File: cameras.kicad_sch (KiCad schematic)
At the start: 30 parts

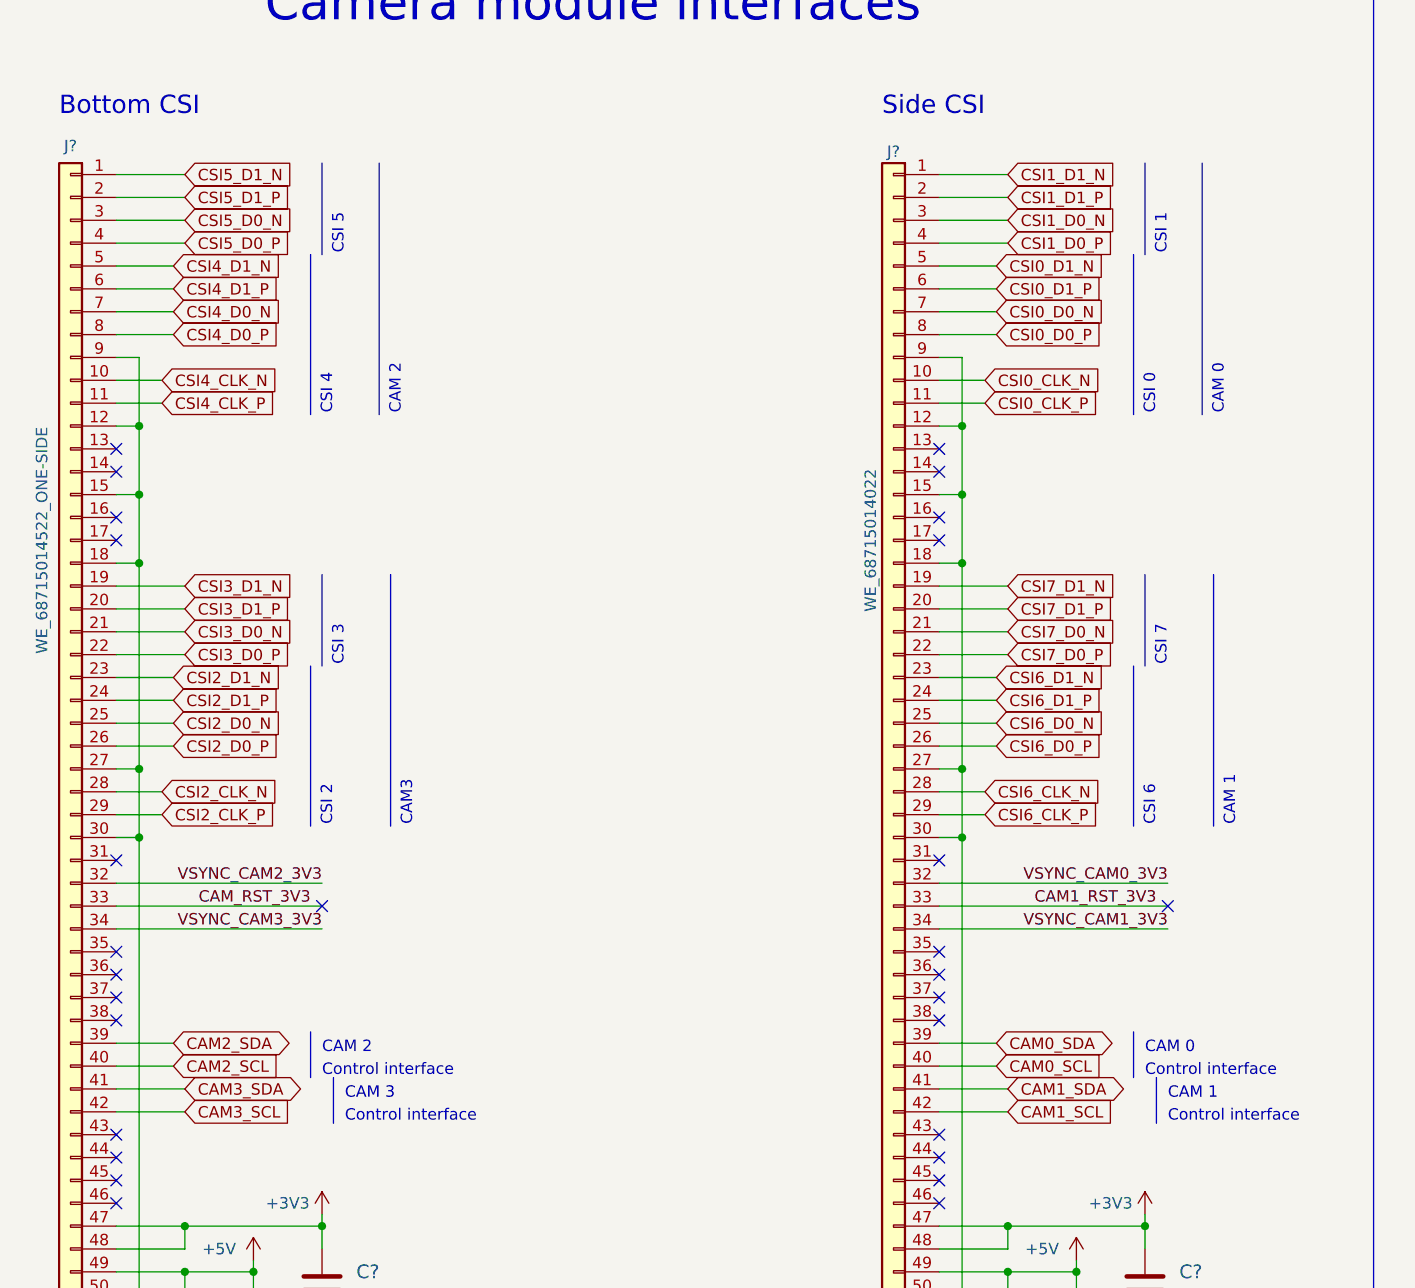
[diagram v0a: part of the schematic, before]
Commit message: Changed pinout to match Jetson Nano Baseboard
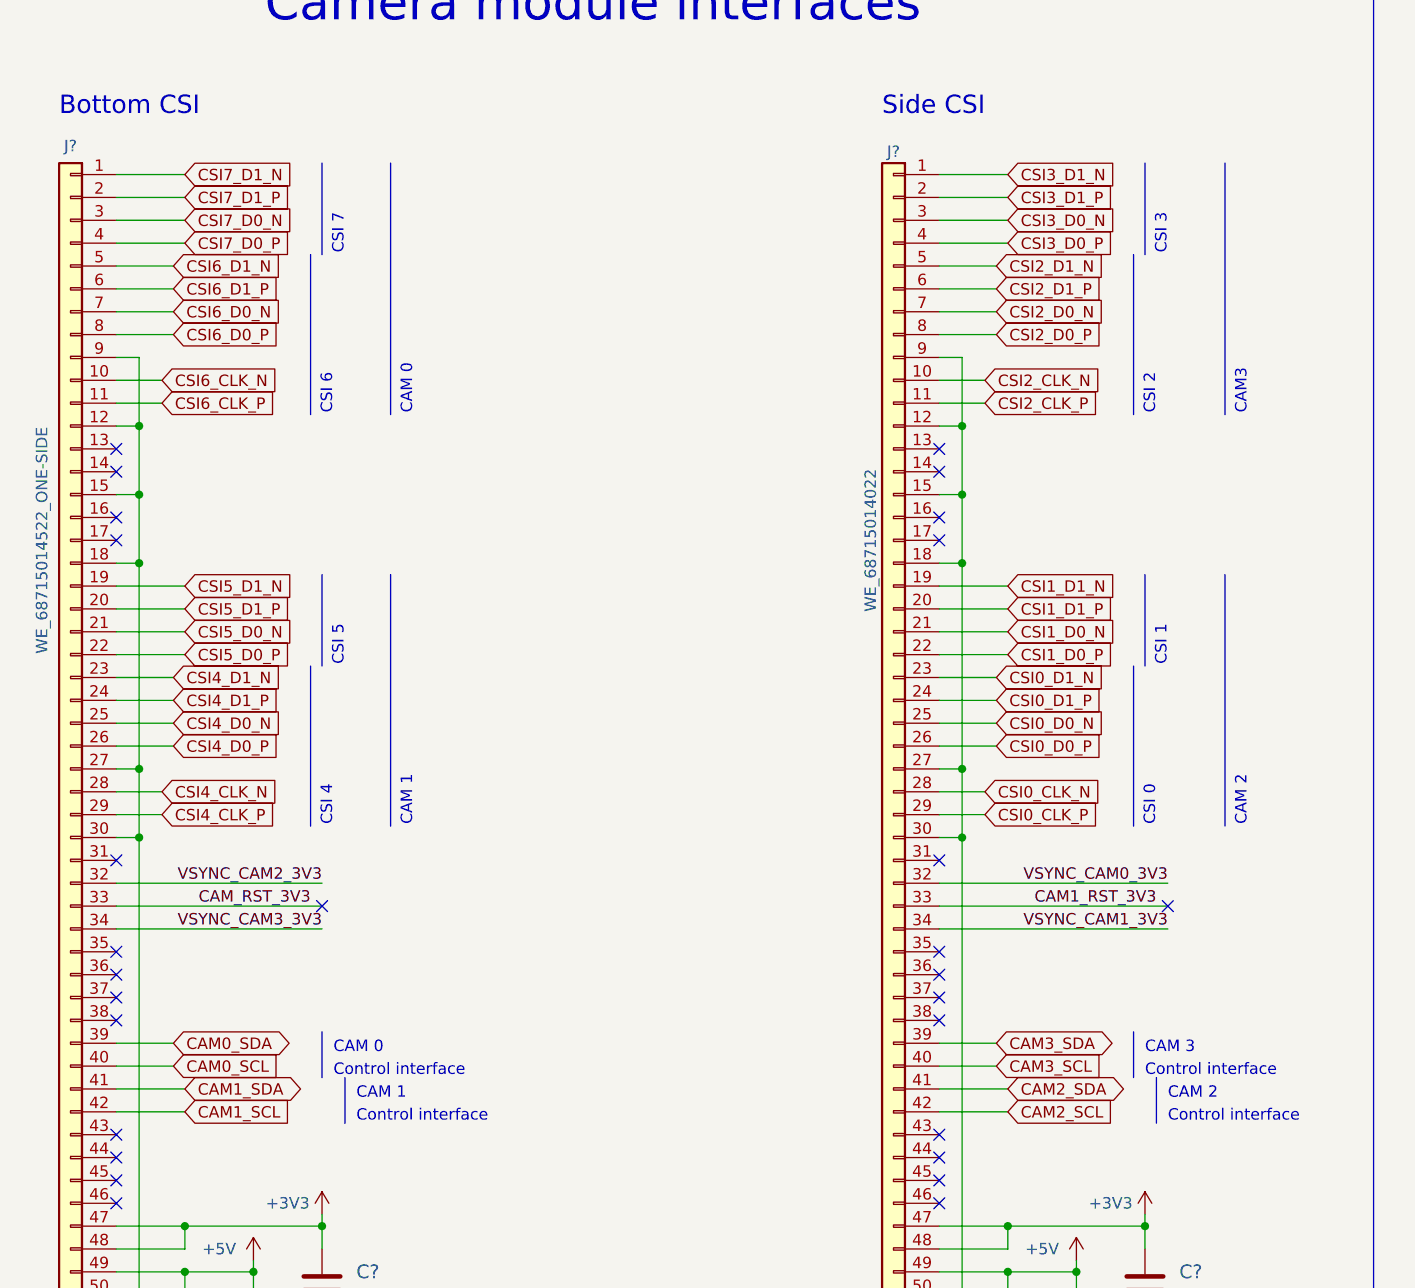
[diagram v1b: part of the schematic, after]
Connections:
- net CAM0_SCL: now also J?.40 (Pin_40); no longer J?.40 (Pin_40)
- net CAM0_SDA: now also J?.39 (Pin_39); no longer J?.39 (Pin_39)
- net CAM1_SCL: now also J?.42 (Pin_42); no longer J?.42 (Pin_42)
- net CAM1_SDA: now also J?.41 (Pin_41); no longer J?.41 (Pin_41)
- net CAM2_SCL: now also J?.42 (Pin_42); no longer J?.40 (Pin_40)
- net CAM2_SDA: now also J?.41 (Pin_41); no longer J?.39 (Pin_39)
- net CAM3_SCL: now also J?.40 (Pin_40); no longer J?.42 (Pin_42)
- net CAM3_SDA: now also J?.39 (Pin_39); no longer J?.41 (Pin_41)
- net CSI0_CLK_N: now also J?.28 (Pin_28); no longer J?.10 (Pin_10)
- net CSI0_CLK_P: now also J?.29 (Pin_29); no longer J?.11 (Pin_11)
- net CSI0_D0_N: now also J?.25 (Pin_25); no longer J?.7 (Pin_7)
- net CSI0_D0_P: now also J?.26 (Pin_26); no longer J?.8 (Pin_8)
- net CSI0_D1_N: now also J?.23 (Pin_23); no longer J?.5 (Pin_5)
- net CSI0_D1_P: now also J?.24 (Pin_24); no longer J?.6 (Pin_6)
- net CSI1_D0_N: now also J?.21 (Pin_21); no longer J?.3 (Pin_3)
- net CSI1_D0_P: now also J?.22 (Pin_22); no longer J?.4 (Pin_4)
- net CSI1_D1_N: now also J?.19 (Pin_19); no longer J?.1 (Pin_1)
- net CSI1_D1_P: now also J?.20 (Pin_20); no longer J?.2 (Pin_2)
- net CSI2_CLK_N: now also J?.10 (Pin_10); no longer J?.28 (Pin_28)
- net CSI2_CLK_P: now also J?.11 (Pin_11); no longer J?.29 (Pin_29)
- net CSI2_D0_N: now also J?.7 (Pin_7); no longer J?.25 (Pin_25)
- net CSI2_D0_P: now also J?.8 (Pin_8); no longer J?.26 (Pin_26)
- net CSI2_D1_N: now also J?.5 (Pin_5); no longer J?.23 (Pin_23)
- net CSI2_D1_P: now also J?.6 (Pin_6); no longer J?.24 (Pin_24)
- net CSI3_D0_N: now also J?.3 (Pin_3); no longer J?.21 (Pin_21)
- net CSI3_D0_P: now also J?.4 (Pin_4); no longer J?.22 (Pin_22)
- net CSI3_D1_N: now also J?.1 (Pin_1); no longer J?.19 (Pin_19)
- net CSI3_D1_P: now also J?.2 (Pin_2); no longer J?.20 (Pin_20)
- net CSI4_CLK_N: now also J?.28 (Pin_28); no longer J?.10 (Pin_10)
- net CSI4_CLK_P: now also J?.29 (Pin_29); no longer J?.11 (Pin_11)
- net CSI4_D0_N: now also J?.25 (Pin_25); no longer J?.7 (Pin_7)
- net CSI4_D0_P: now also J?.26 (Pin_26); no longer J?.8 (Pin_8)
- net CSI4_D1_N: now also J?.23 (Pin_23); no longer J?.5 (Pin_5)
- net CSI4_D1_P: now also J?.24 (Pin_24); no longer J?.6 (Pin_6)
- net CSI5_D0_N: now also J?.21 (Pin_21); no longer J?.3 (Pin_3)
- net CSI5_D0_P: now also J?.22 (Pin_22); no longer J?.4 (Pin_4)
- net CSI5_D1_N: now also J?.19 (Pin_19); no longer J?.1 (Pin_1)
- net CSI5_D1_P: now also J?.20 (Pin_20); no longer J?.2 (Pin_2)
- net CSI6_CLK_N: now also J?.10 (Pin_10); no longer J?.28 (Pin_28)
- net CSI6_CLK_P: now also J?.11 (Pin_11); no longer J?.29 (Pin_29)
- net CSI6_D0_N: now also J?.7 (Pin_7); no longer J?.25 (Pin_25)
- net CSI6_D0_P: now also J?.8 (Pin_8); no longer J?.26 (Pin_26)
- net CSI6_D1_N: now also J?.5 (Pin_5); no longer J?.23 (Pin_23)
- net CSI6_D1_P: now also J?.6 (Pin_6); no longer J?.24 (Pin_24)
- net CSI7_D0_N: now also J?.3 (Pin_3); no longer J?.21 (Pin_21)
- net CSI7_D0_P: now also J?.4 (Pin_4); no longer J?.22 (Pin_22)
- net CSI7_D1_N: now also J?.1 (Pin_1); no longer J?.19 (Pin_19)
- net CSI7_D1_P: now also J?.2 (Pin_2); no longer J?.20 (Pin_20)

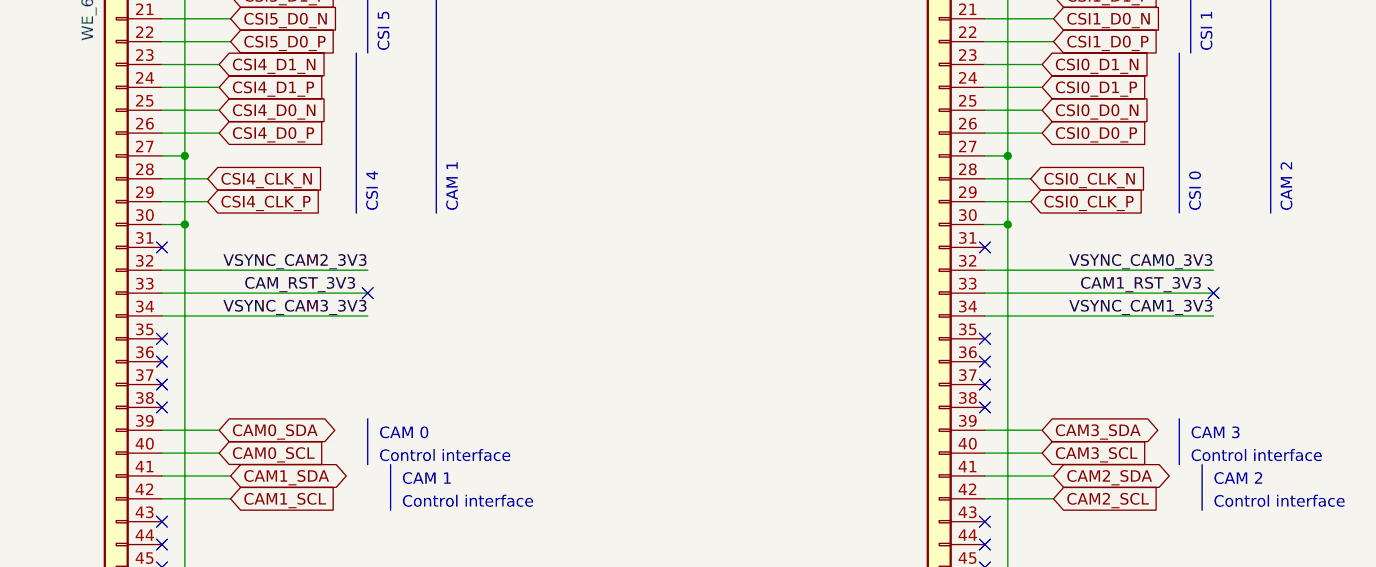
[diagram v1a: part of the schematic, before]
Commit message: Fixed sync pin naming
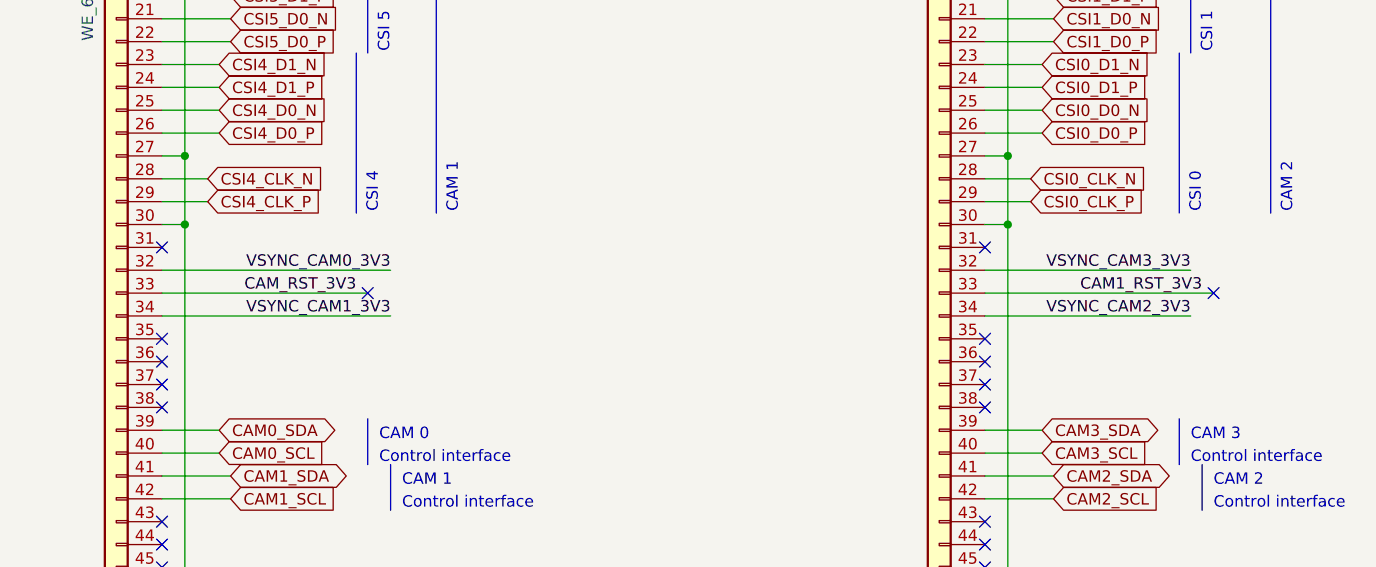
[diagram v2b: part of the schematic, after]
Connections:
- net VSYNC_CAM0_3V3: now also J?.32 (Pin_32); no longer J?.32 (Pin_32)
- net VSYNC_CAM1_3V3: now also J?.34 (Pin_34); no longer J?.34 (Pin_34)
- net VSYNC_CAM2_3V3: now also J?.34 (Pin_34); no longer J?.32 (Pin_32)
- net VSYNC_CAM3_3V3: now also J?.32 (Pin_32); no longer J?.34 (Pin_34)
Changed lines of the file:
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@@
     (stroke (width 0) (type default) (color 0 0 0 0))
   )
-  (wire (pts (xy 142.24 129.54) (xy 167.64 129.54))
+  (wire (pts (xy 50.8 129.54) (xy 76.2 129.54))
     (stroke (width 0) (type default) (color 0 0 0 0))
   )
@@
     (stroke (width 0) (type default) (color 0 0 0 0))
   )
-  (wire (pts (xy 50.8 129.54) (xy 73.66 129.54))
+  (wire (pts (xy 142.24 134.62) (xy 165.1 134.62))
     (stroke (width 0) (type default) (color 0 0 0 0))
   )
@@
     (stroke (width 0) (type default) (color 0 0 0 0))
   )
-  (wire (pts (xy 142.24 134.62) (xy 167.64 134.62))
+  (wire (pts (xy 50.8 134.62) (xy 76.2 134.62))
     (stroke (width 0) (type default) (color 0 0 0 0))
   )
@@
     (stroke (width 0) (type default) (color 0 0 0 0))
   )
-  (wire (pts (xy 50.8 134.62) (xy 73.66 134.62))
+  (wire (pts (xy 142.24 129.54) (xy 165.1 129.54))
     (stroke (width 0) (type default) (color 0 0 0 0))
   )
@@
     (effects (font (size 1.27 1.27)) (justify left bottom))
   )
-  (label "VSYNC_CAM1_3V3" (at 167.64 134.62 180)
+  (label "VSYNC_CAM1_3V3" (at 76.2 134.62 180)
     (effects (font (size 1.27 1.27)) (justify right bottom))
   )
@@
     (effects (font (size 1.27 1.27)) (justify right bottom))
   )
-  (label "VSYNC_CAM0_3V3" (at 167.64 129.54 180)
+  (label "VSYNC_CAM0_3V3" (at 76.2 129.54 180)
     (effects (font (size 1.27 1.27)) (justify right bottom))
   )
@@
     (effects (font (size 1.27 1.27)) (justify right bottom))
   )
-  (label "VSYNC_CAM3_3V3" (at 73.66 134.62 180)
+  (label "VSYNC_CAM3_3V3" (at 165.1 129.54 180)
     (effects (font (size 1.27 1.27)) (justify right bottom))
   )
@@
     (effects (font (size 1.27 1.27)) (justify left bottom))
   )
-  (label "VSYNC_CAM2_3V3" (at 73.66 129.54 180)
+  (label "VSYNC_CAM2_3V3" (at 165.1 134.62 180)
     (effects (font (size 1.27 1.27)) (justify right bottom))
   )
